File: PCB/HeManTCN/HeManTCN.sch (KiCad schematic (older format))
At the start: 110 parts, among them J101 VBATG, J102 VBAT+, J103 Micro_SD_Card, J104 Conn_02x03_Odd_Even, J105 Conn_02x02_Odd_Even, J106 Conn_02x05_Odd_Even, J107 Conn_02x12_Odd_Even, J108 Conn_02x12_Odd_Even, J109 Conn_02x05_Odd_Even, J110 Conn_02x12_Odd_Even, J111 USB_B, J112 USB_B, J113 73725-0110BLF, J114 Screw_Terminal_01x06, J115 RJ45_Amphenol_RJMG1BD3B8K1ANR, J116 Screw_Terminal_01x02, SW101 RESET, SW102 PC13, U101 STM32H743VITx, U102 MVBC02D, U103 S25FL127SABMFI101, U104 STM32F042F6Px, U105 TCAN332, U106 ISL83483, U107 USBLC6-2SC6, U108 KSZ8081RNA, U109 USBLC6-2SC6, U110 USBLC6-2SC6, U111 MIC2005A, U112 AP63203, Y101 8MHz, Y102 32.768KHz, Y103 25MHz

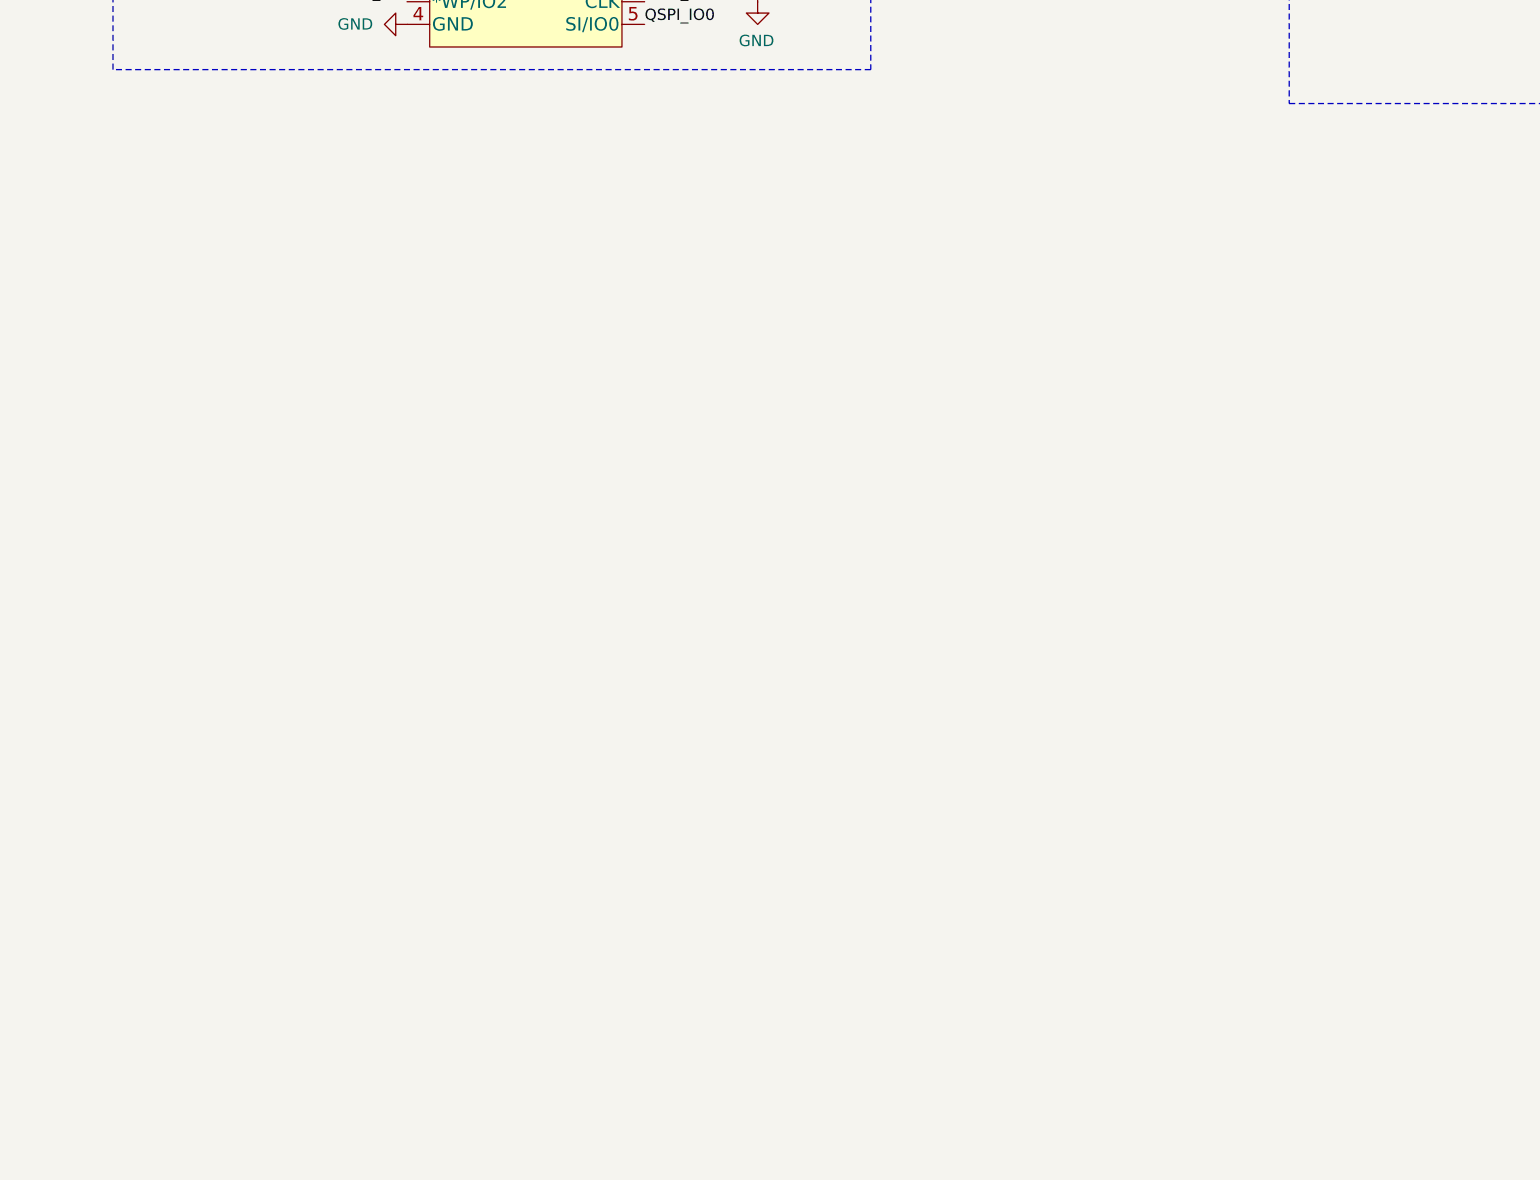
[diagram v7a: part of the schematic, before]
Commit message: Buffers en Esquematico.
Se colocaron los buffers en el esquematico.
Se agregaron las librerias correspondientes y sus footprints.
MVBC02D con pines arreglados.
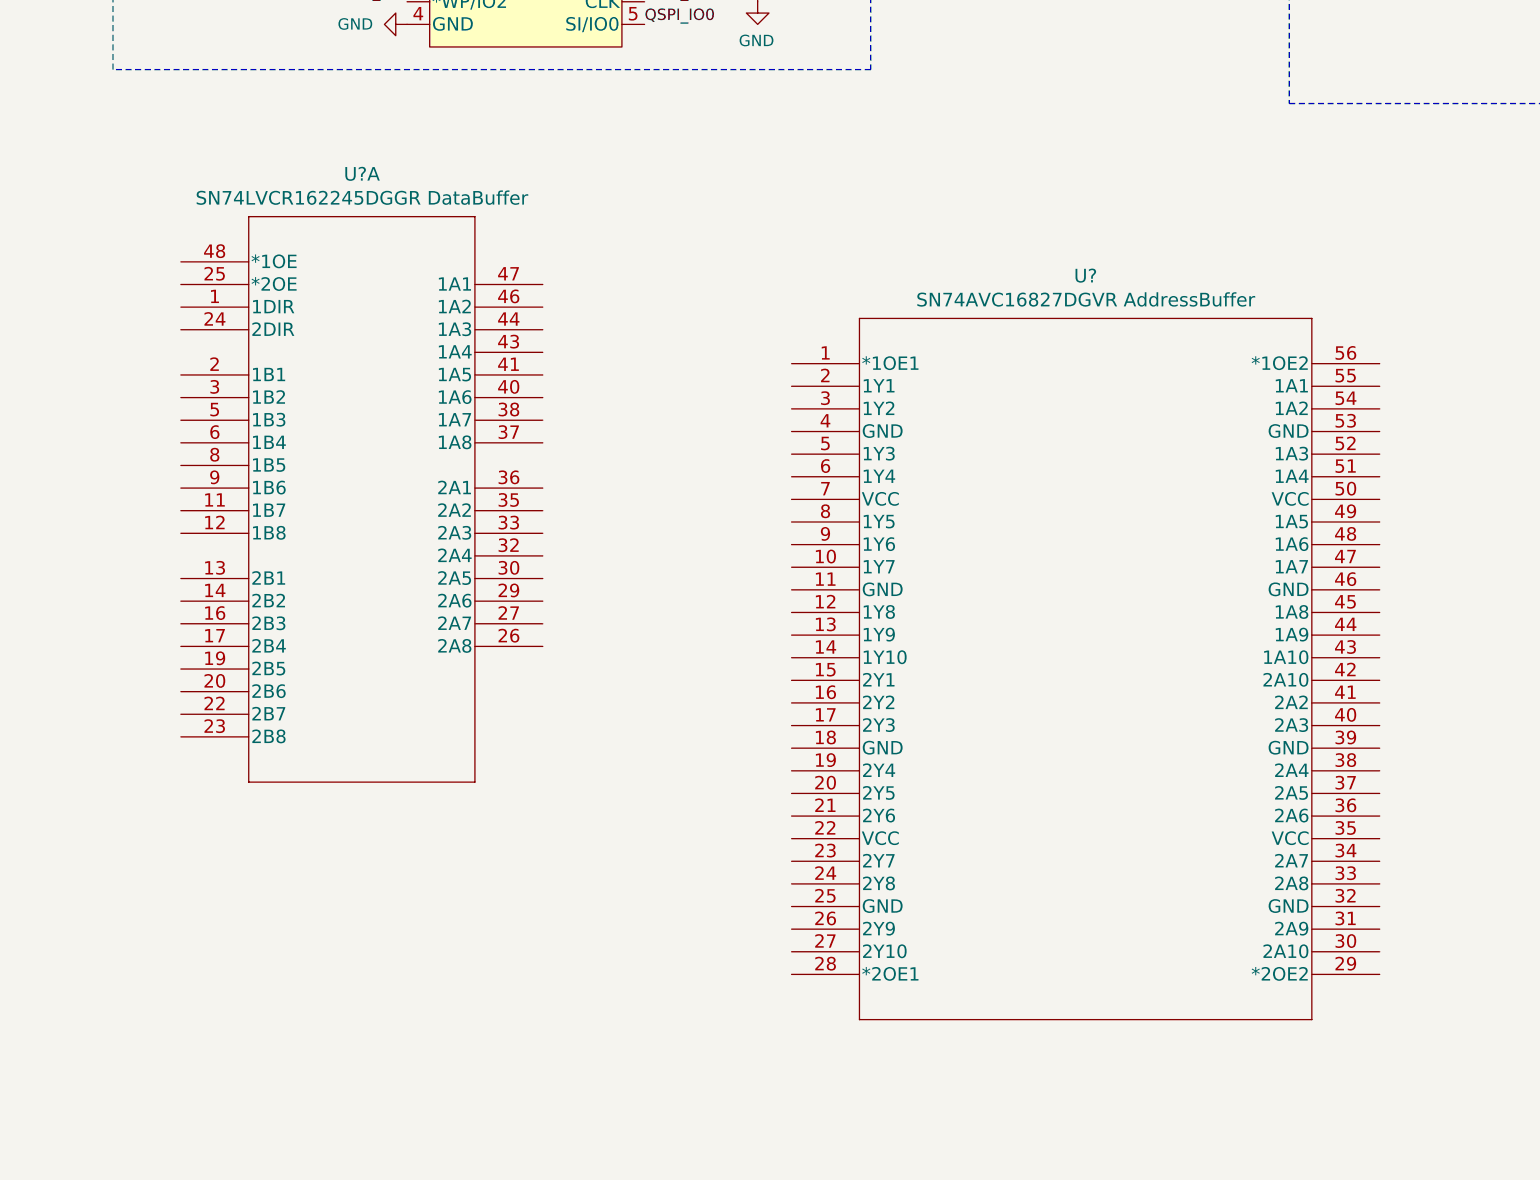
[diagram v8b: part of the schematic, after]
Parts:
- added U?: SN74LVCR162245DGGR DataBuffer, DGG48, symbol 2019-12-04_21-08-15:SN74LVCR162245DGGR
- added U?: SN74AVC16827DGVR AddressBuffer, DGV56, symbol 2019-12-04_21-05-43:SN74AVC16827DGVR
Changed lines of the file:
@@
 Wire Wire Line
 	11200 5650 11600 5650
+$Comp
+L 2019-12-04_21-08-15:SN74LVCR162245DGGR U?
+U 1 1 5E05E3B3
+P 13200 4250
+F 0 "U?" H 14000 4637 60  0000 C CNN
+F 1 "SN74LVCR162245DGGR DataBuffer" H 14000 4531 60  0000 C CNN
+F 2 "DGG48" H 14000 4490 60  0001 C CNN
+F 3 "" H 13200 4250 60  0000 C CNN
+	1    13200 4250
+	1    0    0    -1
+$EndComp
+$Comp
+L 2019-12-04_21-05-43:SN74AVC16827DGVR U?
+U 1 1 5E070B31
+P 15900 4700
+F 0 "U?" H 17200 5087 60  0000 C CNN
+F 1 "SN74AVC16827DGVR AddressBuffer" H 17200 4981 60  0000 C CNN
+F 2 "DGV56" H 17200 4940 60  0001 C CNN
+F 3 "" H 15900 4700 60  0000 C CNN
+	1    15900 4700
+	1    0    0    -1
+$EndComp
 $EndSCHEMATC
